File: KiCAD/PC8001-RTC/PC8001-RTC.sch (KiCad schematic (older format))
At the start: 13 parts, among them J1 PC-8001 ext BUS, J2 ADDR JP, U1 74HC138, U2 RTC7301DG, U3 PST600

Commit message: 回路図修正/PC-8001 サンプルプログラム添付
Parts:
- J2: symbol Connector_Generic:Conn_02x08_Counter_Clockwise -> Connector_Generic:Conn_02x08_Odd_Even
- R1: value 10k -> 10K
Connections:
- net A7: now also RN1.6 (R5); no longer R1.1
- net GND: no longer R1.2
- net VCC: now also R1.1
- net ~IOREQ: now also RN1.5 (R4); no longer RN1.6 (R5)
- net ~RTCCE: now also J2.2 (Pin_2), J2.4 (Pin_4), J2.6 (Pin_6), J2.8 (Pin_8); no longer J2.11 (Pin_11), J2.13 (Pin_13), J2.15 (Pin_15), J2.9 (Pin_9)
- net at U2.15 (CS1), U3.3 (OUT): now also R1.2
- net at U1.10 (O5): now also J2.11 (Pin_11); no longer J2.6 (Pin_6)
- net at U1.11 (O4): now also J2.9 (Pin_9); no longer J2.5 (Pin_5)
- net at U1.12 (O3): now also J2.7 (Pin_7); no longer J2.4 (Pin_4)
- net at U1.13 (O2): now also J2.5 (Pin_5); no longer J2.3 (Pin_3)
- net at U1.14 (O1): now also J2.3 (Pin_3); no longer J2.2 (Pin_2)
- net at U1.7 (O7): now also J2.15 (Pin_15); no longer J2.8 (Pin_8)
- net at U1.9 (O6): now also J2.13 (Pin_13); no longer J2.7 (Pin_7)
- no-connect marks 38 -> 37
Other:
- note added: "$8x"
- note added: "$9x"
- note added: "$Ax"
- note added: "$Bx"
- note added: "$Cx"
- note added: "$Dx"
- note added: "$Ex"
- note added: "$Fx"
- note added: "Supercapacitor"
- moved on the sheet: J2
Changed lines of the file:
@@
 EESchema Schematic File Version 4
-EELAYER 30 0
+LIBS:PC8001-RTC-cache
+EELAYER 26 0
 EELAYER END
 $Descr A4 11693 8268
@@
 A6
 $Comp
-L Connector_Generic:Conn_02x08_Counter_Clockwise J2
+L Connector_Generic:Conn_02x08_Odd_Even J2
 U 1 1 5E1D9D73
-P 6800 4250
-F 0 "J2" H 6850 4767 50  0000 C CNN
-F 1 "ADDR JP" H 6850 4676 50  0000 C CNN
-F 2 "" H 6800 4250 50  0001 C CNN
-F 3 "~" H 6800 4250 50  0001 C CNN
-	1    6800 4250
-	1    0    0    -1
-$EndComp
-Wire Wire Line
-	7100 3950 7200 3950
+P 6850 4250
+F 0 "J2" H 6900 4767 50  0000 C CNN
+F 1 "ADDR JP" H 6900 4676 50  0000 C CNN
+F 2 "" H 6850 4250 50  0001 C CNN
+F 3 "~" H 6850 4250 50  0001 C CNN
+	1    6850 4250
+	1    0    0    -1
+$EndComp
+Wire Wire Line
+	7150 3950 7200 3950
 Wire Wire Line
 	7200 3950 7200 4050
 Wire Wire Line
-	7200 4650 7100 4650
+	7200 4650 7150 4650
 Connection ~ 7200 3950
 Wire Wire Line
 	7200 3950 8350 3950
 Wire Wire Line
-	7100 4050 7200 4050
+	7150 4050 7200 4050
 Connection ~ 7200 4050
 Wire Wire Line
 	7200 4050 7200 4150
 Wire Wire Line
-	7100 4150 7200 4150
+	7150 4150 7200 4150
 Connection ~ 7200 4150
 Wire Wire Line
 	7200 4150 7200 4250
 Wire Wire Line
-	7100 4250 7200 4250
+	7150 4250 7200 4250
 Connection ~ 7200 4250
 Wire Wire Line
 	7200 4250 7200 4350
 Wire Wire Line
-	7100 4350 7200 4350
+	7150 4350 7200 4350
 Connection ~ 7200 4350
 Wire Wire Line
 	7200 4350 7200 4450
 Wire Wire Line
-	7200 4450 7100 4450
+	7200 4450 7150 4450
 Connection ~ 7200 4450
 Wire Wire Line
 	7200 4450 7200 4550
 Wire Wire Line
-	7100 4550 7200 4550
+	7150 4550 7200 4550
 Connection ~ 7200 4550
 Wire Wire Line
 	7200 4550 7200 4650
 Wire Wire Line
-	6500 3950 6600 3950
-Wire Wire Line
-	6500 4050 6600 4050
-Wire Wire Line
-	6500 4150 6600 4150
-Wire Wire Line
-	6500 4250 6600 4250
-Wire Wire Line
-	6500 4350 6600 4350
-Wire Wire Line
-	6500 4450 6600 4450
-Wire Wire Line
-	6500 4550 6600 4550
-Wire Wire Line
-	6500 4650 6600 4650
+	6500 3950 6650 3950
+Wire Wire Line
+	6500 4050 6650 4050
+Wire Wire Line
+	6500 4150 6650 4150
+Wire Wire Line
+	6500 4250 6650 4250
+Wire Wire Line
+	6500 4350 6650 4350
+Wire Wire Line
+	6500 4450 6650 4450
+Wire Wire Line
+	6500 4550 6650 4550
+Wire Wire Line
+	6500 4650 6650 4650
 NoConn ~ 9150 5100
 NoConn ~ 9150 5200
@@
 Wire Wire Line
 	4750 3150 4750 3400
-Wire Wire Line
-	4850 4450 5250 4450
-Wire Wire Line
-	4750 4550 5150 4550
-Wire Wire Line
-	5150 3800 5150 4550
-Connection ~ 5150 4550
-Wire Wire Line
-	5150 4550 5500 4550
-NoConn ~ 5050 3800
-$Comp
-L Device:R_US R1
-U 1 1 5E39FEE7
-P 5250 4800
-F 0 "R1" H 5100 4850 50  0000 L CNN
-F 1 "10k" H 5050 4750 50  0000 L CNN
-F 2 "" V 5290 4790 50  0001 C CNN
-F 3 "~" H 5250 4800 50  0001 C CNN
-	1    5250 4800
-	1    0    0    -1
-$EndComp
-Wire Wire Line
-	5250 4450 5250 4650
-Connection ~ 5250 4450
-Wire Wire Line
-	5250 4450 5500 4450
-Wire Wire Line
-	5250 4950 5250 5000
-Wire Wire Line
-	5250 5000 5400 5000
-Connection ~ 5400 5000
 $Comp
 L Device:D_Schottky D1
@@
 P 7750 2350
 F 0 "D2" V 7704 2429 50  0000 L CNN
-F 1 "1N4148" V 7800 2000 50  0000 L CNN
+F 1 "1N4148" V 7850 2200 50  0000 L CNN
 F 2 "" H 7750 2350 50  0001 C CNN
 F 3 "~" H 7750 2350 50  0001 C CNN
@@
 	6900 3000 6900 3050
 Wire Wire Line
-	7500 2600 7250 2600
+	7500 2600 7350 2600
 NoConn ~ 2950 2450
 NoConn ~ 2950 2550
@@
 Wire Wire Line
 	8450 2100 8650 2100
+Wire Wire Line
+	4850 4450 5150 4450
+Wire Wire Line
+	4750 4550 5050 4550
+Wire Wire Line
+	5050 3800 5050 4550
+Connection ~ 5050 4550
+Wire Wire Line
+	5050 4550 5500 4550
+Wire Wire Line
+	5150 3800 5150 4450
+Connection ~ 5150 4450
+Wire Wire Line
+	5150 4450 5500 4450
+$Comp
+L Device:R_US R1
+U 1 1 5E1ED6C7
+P 7350 2350
+F 0 "R1" H 7200 2400 50  0000 L CNN
+F 1 "10K" H 7150 2300 50  0000 L CNN
+F 2 "" V 7390 2340 50  0001 C CNN
+F 3 "~" H 7350 2350 50  0001 C CNN
+	1    7350 2350
+	1    0    0    -1
+$EndComp
+Wire Wire Line
+	7350 2200 7350 2100
+Connection ~ 7350 2100
+Wire Wire Line
+	7350 2500 7350 2600
+Connection ~ 7350 2600
+Wire Wire Line
+	7350 2600 7250 2600
+Text Notes 6500 3950 0    50   ~ 0
+$8x
+Text Notes 6500 4050 0    50   ~ 0
+$9x
+Text Notes 6500 4150 0    50   ~ 0
+$Ax
+Text Notes 6500 4250 0    50   ~ 0
+$Bx
+Text Notes 6500 4350 0    50   ~ 0
+$Cx
+Text Notes 6500 4450 0    50   ~ 0
+$Dx
+Text Notes 6500 4550 0    50   ~ 0
+$Ex
+Text Notes 6500 4650 0    50   ~ 0
+$Fx
+Text Notes 8400 2650 0    50   ~ 0
+Supercapacitor
 $EndSCHEMATC

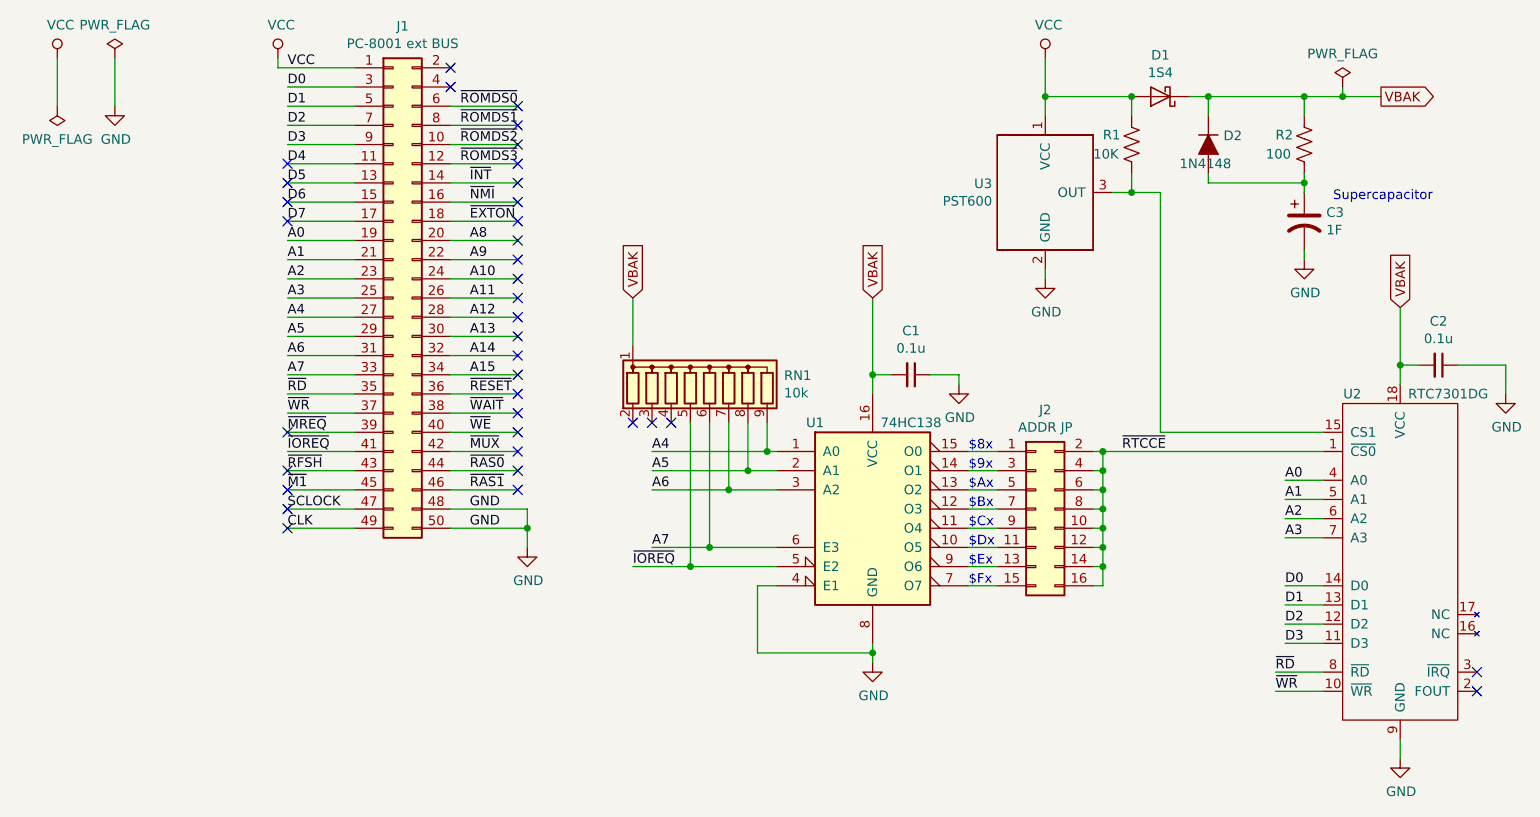
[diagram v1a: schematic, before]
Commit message: バックアップ電源回路見直しなど
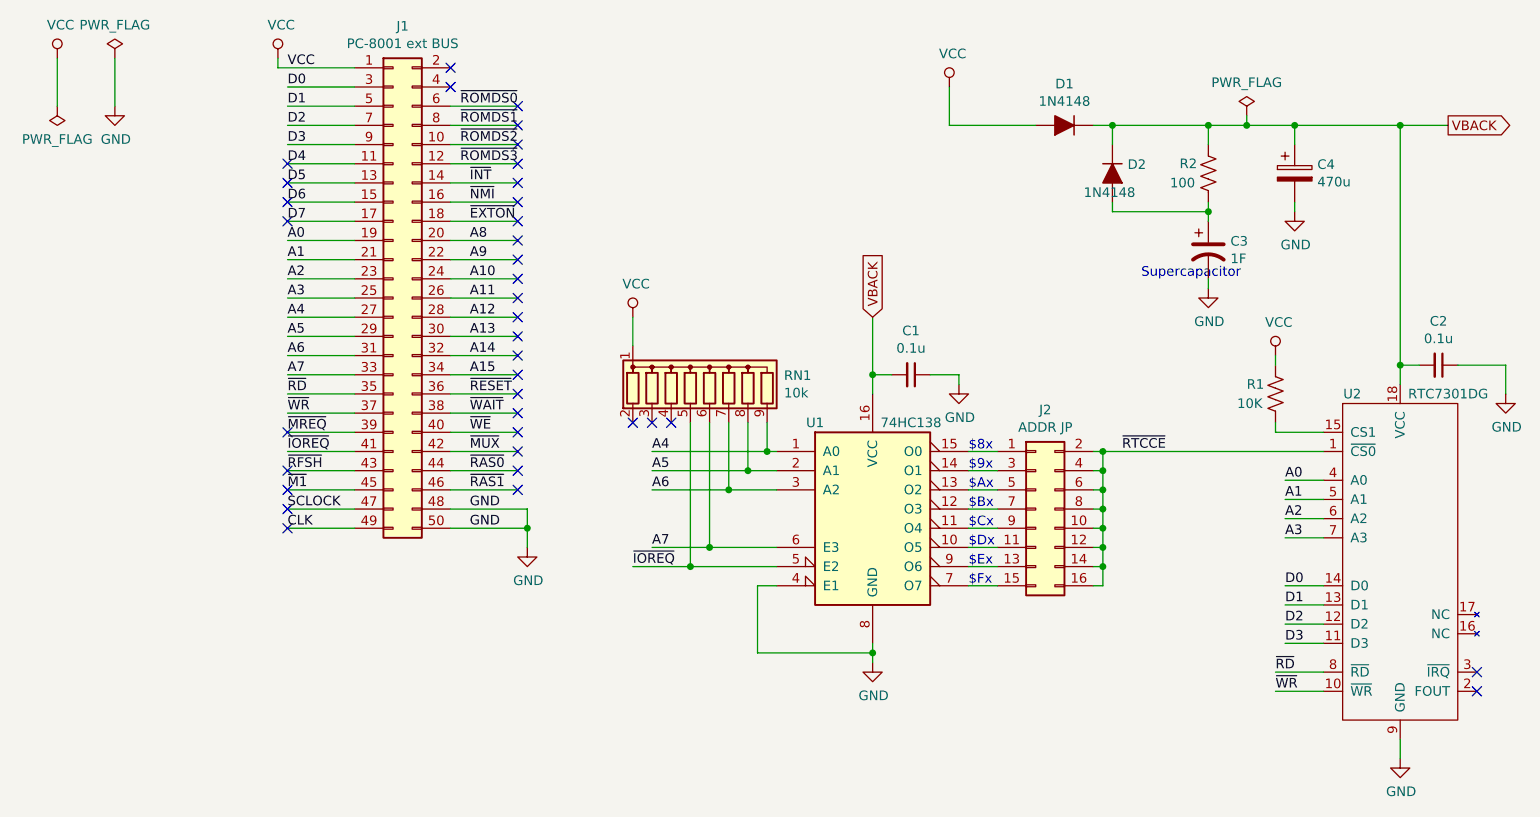
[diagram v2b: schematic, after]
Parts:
- removed D1: 1S4, symbol Device:D_Schottky
- removed U3: PST600, symbol PST600:PST600
- added C4: 470u, symbol Device:CP
- added D1: 1N4148, symbol Device:D_ALT
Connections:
- net GND: now also C4.2
- net VCC: now also RN1.1 (common), D1.2 (A)
- net VBAK renamed VBACK
- net VBACK: now also C4.1, D1.1 (K); no longer RN1.1 (common)
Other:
- moved on the sheet: C3, D2, R1, R2
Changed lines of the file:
@@
 EESchema Schematic File Version 4
 LIBS:PC8001-RTC-cache
-EELAYER 26 0
+EELAYER 30 0
 EELAYER END
 $Descr A4 11693 8268
@@
 	1    0    0    -1
 $EndComp
-Wire Wire Line
-	8750 3200 8750 3500
 $Comp
 L power:GND #PWR010
@@
 ~RTCCE
 Wire Wire Line
-	7500 3850 8350 3850
+	8100 3850 8350 3850
 $Comp
 L 74xx:74LS138 U1
@@
 $EndComp
 Wire Wire Line
-	6000 3150 6000 3550
+	6000 3250 6000 3550
 Wire Wire Line
 	6000 3550 6100 3550
@@
 	7200 4650 7150 4650
 Connection ~ 7200 3950
-Wire Wire Line
-	7200 3950 8350 3950
 Wire Wire Line
 	7150 4050 7200 4050
@@
 L power:VCC #PWR05
 U 1 1 5E31E580
-P 6900 1900
-F 0 "#PWR05" H 6900 1750 50  0001 C CNN
-F 1 "VCC" H 6917 2073 50  0000 C CNN
-F 2 "" H 6900 1900 50  0001 C CNN
-F 3 "" H 6900 1900 50  0001 C CNN
-	1    6900 1900
+P 6400 2050
+F 0 "#PWR05" H 6400 1900 50  0001 C CNN
+F 1 "VCC" H 6417 2223 50  0000 C CNN
+F 2 "" H 6400 2050 50  0001 C CNN
+F 3 "" H 6400 2050 50  0001 C CNN
+	1    6400 2050
 	1    0    0    -1
 $EndComp
@@
 	5250 4150 5500 4150
 Wire Wire Line
-	4750 3150 4750 3400
-$Comp
-L Device:D_Schottky D1
-U 1 1 5E3E94B6
-P 7500 2100
-F 0 "D1" H 7500 1884 50  0000 C CNN
-F 1 "1S4" H 7500 1975 50  0000 C CNN
-F 2 "" H 7500 2100 50  0001 C CNN
-F 3 "~" H 7500 2100 50  0001 C CNN
-	1    7500 2100
-	-1   0    0    1
-$EndComp
-Wire Wire Line
-	6900 1900 6900 2100
-Wire Wire Line
-	6900 2100 7350 2100
+	6400 2050 6400 2250
+Wire Wire Line
+	6400 2250 6850 2250
 $Comp
 L Device:D_ALT D2
 U 1 1 5E4135CD
-P 7750 2350
-F 0 "D2" V 7704 2429 50  0000 L CNN
-F 1 "1N4148" V 7850 2200 50  0000 L CNN
-F 2 "" H 7750 2350 50  0001 C CNN
-F 3 "~" H 7750 2350 50  0001 C CNN
-	1    7750 2350
+P 7250 2500
+F 0 "D2" V 7204 2579 50  0000 L CNN
+F 1 "1N4148" V 7350 2350 50  0000 L CNN
+F 2 "" H 7250 2500 50  0001 C CNN
+F 3 "~" H 7250 2500 50  0001 C CNN
+	1    7250 2500
 	0    1    1    0
 $EndComp
@@
 L Device:R_US R2
 U 1 1 5E413A26
-P 8250 2350
-F 0 "R2" H 8100 2400 50  0000 L CNN
-F 1 "100" H 8050 2300 50  0000 L CNN
-F 2 "" V 8290 2340 50  0001 C CNN
-F 3 "~" H 8250 2350 50  0001 C CNN
-	1    8250 2350
+P 7750 2500
+F 0 "R2" H 7600 2550 50  0000 L CNN
+F 1 "100" H 7550 2450 50  0000 L CNN
+F 2 "" V 7790 2490 50  0001 C CNN
+F 3 "~" H 7750 2500 50  0001 C CNN
+	1    7750 2500
 	1    0    0    -1
 $EndComp
@@
 L Device:CP1 C3
 U 1 1 5E41B21F
-P 8250 2750
-F 0 "C3" H 8365 2796 50  0000 L CNN
-F 1 "1F" H 8365 2705 50  0000 L CNN
-F 2 "" H 8250 2750 50  0001 C CNN
-F 3 "~" H 8250 2750 50  0001 C CNN
-	1    8250 2750
-	1    0    0    -1
-$EndComp
-Wire Wire Line
-	7750 2500 7750 2550
-Wire Wire Line
-	7750 2550 8250 2550
-Wire Wire Line
-	8250 2550 8250 2500
-Wire Wire Line
-	8250 2550 8250 2600
-Connection ~ 8250 2550
-Wire Wire Line
-	7650 2100 7750 2100
-Wire Wire Line
-	7750 2100 7750 2200
-Connection ~ 7750 2100
-Wire Wire Line
-	7750 2100 8250 2100
-Wire Wire Line
-	8250 2100 8250 2200
-Connection ~ 8250 2100
-Wire Wire Line
-	8250 2100 8450 2100
+P 7750 2900
+F 0 "C3" H 7865 2946 50  0000 L CNN
+F 1 "1F" H 7865 2855 50  0000 L CNN
+F 2 "" H 7750 2900 50  0001 C CNN
+F 3 "~" H 7750 2900 50  0001 C CNN
+	1    7750 2900
+	1    0    0    -1
+$EndComp
+Wire Wire Line
+	7250 2650 7250 2700
+Wire Wire Line
+	7250 2700 7750 2700
+Wire Wire Line
+	7750 2700 7750 2650
+Wire Wire Line
+	7750 2700 7750 2750
+Connection ~ 7750 2700
+Wire Wire Line
+	7150 2250 7250 2250
+Wire Wire Line
+	7250 2250 7250 2350
+Connection ~ 7250 2250
+Wire Wire Line
+	7250 2250 7750 2250
+Wire Wire Line
+	7750 2250 7750 2350
+Connection ~ 7750 2250
+Wire Wire Line
+	7750 2250 7950 2250
 $Comp
 L power:GND #PWR09
 U 1 1 5E43D1F9
-P 8250 2950
-F 0 "#PWR09" H 8250 2700 50  0001 C CNN
-F 1 "GND" H 8255 2777 50  0000 C CNN
-F 2 "" H 8250 2950 50  0001 C CNN
-F 3 "" H 8250 2950 50  0001 C CNN
-	1    8250 2950
-	1    0    0    -1
-$EndComp
-Wire Wire Line
-	8250 2900 8250 2950
+P 7750 3100
+F 0 "#PWR09" H 7750 2850 50  0001 C CNN
+F 1 "GND" H 7755 2927 50  0000 C CNN
+F 2 "" H 7750 3100 50  0001 C CNN
+F 3 "" H 7750 3100 50  0001 C CNN
+	1    7750 3100
+	1    0    0    -1
+$EndComp
+Wire Wire Line
+	7750 3050 7750 3100
 Wire Wire Line
 	8750 5450 8750 5550
-Wire Wire Line
-	7500 2600 7500 3850
-$Comp
-L PST600:PST600 U3
-U 1 1 5E46096B
-P 6900 2600
-F 0 "U3" H 6623 2646 50  0000 R CNN
-F 1 "PST600" H 6623 2555 50  0000 R CNN
-F 2 "" H 6900 2600 50  0001 C CNN
-F 3 "" H 6900 2600 50  0001 C CNN
-	1    6900 2600
-	1    0    0    -1
-$EndComp
-Wire Wire Line
-	6900 2100 6900 2200
-Connection ~ 6900 2100
-$Comp
-L power:GND #PWR08
-U 1 1 5E46E494
-P 6900 3050
-F 0 "#PWR08" H 6900 2800 50  0001 C CNN
-F 1 "GND" H 6905 2877 50  0000 C CNN
-F 2 "" H 6900 3050 50  0001 C CNN
-F 3 "" H 6900 3050 50  0001 C CNN
-	1    6900 3050
-	1    0    0    -1
-$EndComp
-Wire Wire Line
-	6900 3000 6900 3050
-Wire Wire Line
-	7500 2600 7350 2600
 NoConn ~ 2950 2450
 NoConn ~ 2950 2550
 NoConn ~ 2950 2650
 NoConn ~ 2950 2750
-Text GLabel 8650 2100 2    50   Output ~ 0
-VBAK
-Text GLabel 4750 3150 1    50   Input ~ 0
-VBAK
-Text GLabel 6000 3150 1    50   Input ~ 0
-VBAK
-Text GLabel 8750 3200 1    50   Input ~ 0
-VBAK
 $Comp
 L power:PWR_FLAG #FLG0101
 U 1 1 5E4DD9E9
-P 8450 2050
-F 0 "#FLG0101" H 8450 2125 50  0001 C CNN
-F 1 "PWR_FLAG" H 8450 2223 50  0000 C CNN
-F 2 "" H 8450 2050 50  0001 C CNN
-F 3 "~" H 8450 2050 50  0001 C CNN
-	1    8450 2050
-	1    0    0    -1
-$EndComp
-Wire Wire Line
-	8450 2050 8450 2100
-Connection ~ 8450 2100
-Wire Wire Line
-	8450 2100 8650 2100
+P 7950 2200
+F 0 "#FLG0101" H 7950 2275 50  0001 C CNN
+F 1 "PWR_FLAG" H 7950 2373 50  0000 C CNN
+F 2 "" H 7950 2200 50  0001 C CNN
+F 3 "~" H 7950 2200 50  0001 C CNN
+	1    7950 2200
+	1    0    0    -1
+$EndComp
+Wire Wire Line
+	7950 2200 7950 2250
+Connection ~ 7950 2250
+Wire Wire Line
+	7950 2250 8200 2250
 Wire Wire Line
 	4850 4450 5150 4450
@@
 L Device:R_US R1
 U 1 1 5E1ED6C7
-P 7350 2350
-F 0 "R1" H 7200 2400 50  0000 L CNN
-F 1 "10K" H 7150 2300 50  0000 L CNN
-F 2 "" V 7390 2340 50  0001 C CNN
-F 3 "~" H 7350 2350 50  0001 C CNN
-	1    7350 2350
-	1    0    0    -1
-$EndComp
-Wire Wire Line
-	7350 2200 7350 2100
-Connection ~ 7350 2100
-Wire Wire Line
-	7350 2500 7350 2600
-Connection ~ 7350 2600
-Wire Wire Line
-	7350 2600 7250 2600
+P 8100 3650
+F 0 "R1" H 7950 3700 50  0000 L CNN
+F 1 "10K" H 7900 3600 50  0000 L CNN
+F 2 "" V 8140 3640 50  0001 C CNN
+F 3 "~" H 8100 3650 50  0001 C CNN
+	1    8100 3650
+	1    0    0    -1
+$EndComp
 Text Notes 6500 3950 0    50   ~ 0
 $8x
@@
 Text Notes 6500 4650 0    50   ~ 0
 $Fx
-Text Notes 8400 2650 0    50   ~ 0
+Text Notes 7400 3050 0    50   ~ 0
 Supercapacitor
+Wire Wire Line
+	4750 3250 4750 3400
+$Comp
+L Device:CP C4
+U 1 1 5E38A4C0
+P 8200 2500
+F 0 "C4" H 8318 2546 50  0000 L CNN
+F 1 "470u" H 8318 2455 50  0000 L CNN
+F 2 "" H 8238 2350 50  0001 C CNN
+F 3 "~" H 8200 2500 50  0001 C CNN
+	1    8200 2500
+	1    0    0    -1
+$EndComp
+$Comp
+L power:GND #PWR014
+U 1 1 5E38A5AF
+P 8200 2700
+F 0 "#PWR014" H 8200 2450 50  0001 C CNN
+F 1 "GND" H 8205 2527 50  0000 C CNN
+F 2 "" H 8200 2700 50  0001 C CNN
+F 3 "" H 8200 2700 50  0001 C CNN
+	1    8200 2700
+	1    0    0    -1
+$EndComp
+Wire Wire Line
+	8200 2250 8200 2350
+Connection ~ 8200 2250
+Wire Wire Line
+	8200 2650 8200 2700
+Wire Wire Line
+	8200 2250 8750 2250
+Wire Wire Line
+	8100 3800 8100 3850
+Wire Wire Line
+	7200 3950 8350 3950
+Wire Wire Line
+	8750 2250 8750 3500
+$Comp
+L Device:D_ALT D1
+U 1 1 5E39E3EE
+P 7000 2250
+F 0 "D1" H 7000 2034 50  0000 C CNN
+F 1 "1N4148" H 7000 2125 50  0000 C CNN
+F 2 "" H 7000 2250 50  0001 C CNN
+F 3 "~" H 7000 2250 50  0001 C CNN
+	1    7000 2250
+	-1   0    0    1
+$EndComp
+$Comp
+L power:VCC #PWR08
+U 1 1 5E3B9567
+P 8100 3450
+F 0 "#PWR08" H 8100 3300 50  0001 C CNN
+F 1 "VCC" H 8117 3623 50  0000 C CNN
+F 2 "" H 8100 3450 50  0001 C CNN
+F 3 "" H 8100 3450 50  0001 C CNN
+	1    8100 3450
+	1    0    0    -1
+$EndComp
+Wire Wire Line
+	8100 3450 8100 3500
+Text GLabel 9000 2250 2    50   Output ~ 0
+VBACK
+Wire Wire Line
+	8750 2250 9000 2250
+Connection ~ 8750 2250
+Text GLabel 6000 3250 1    50   Input ~ 0
+VBACK
+$Comp
+L power:VCC #PWR?
+U 1 1 5E3FD736
+P 4750 3250
+F 0 "#PWR?" H 4750 3100 50  0001 C CNN
+F 1 "VCC" H 4767 3423 50  0000 C CNN
+F 2 "" H 4750 3250 50  0001 C CNN
+F 3 "" H 4750 3250 50  0001 C CNN
+	1    4750 3250
+	1    0    0    -1
+$EndComp
 $EndSCHEMATC
